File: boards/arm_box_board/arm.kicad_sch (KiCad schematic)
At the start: 5 parts, among them J1 Output, J2 24V, U1 Teensy4.1, U2 PololuD24V5F5, U3 TMC2209_SILENTSTEPSTICK

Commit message: Updated Arm board with ethernet
updated on 04/24
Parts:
- added C1: C_Small, Capacitor_THT:C_Rect_L4.0mm_W2.5mm_P2.50mm, symbol Device:C_Small
- added J3: J00-0045NL, EthernetConn:PULSE_J00-0045NL, symbol EthernetHead:J00-0045NL
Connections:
- net at U1.60 (R+): now also J3.4 (CTT)
- net at U1.61 (LED): now also J3.10 (LC)
- net at U1.62 (T-): now also J3.3 (RD+)
- net at U1.63 (T+): now also J3.1 (TD+)
- net at U1.64 (GND): now also C1.2, J3.8 (GND), J3.9 (LA)
- net at U1.65 (R-): now also J3.6 (RD-)
- new net: C1.1, J3.2 (TD-), J3.5 (CTR)

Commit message: update
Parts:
- C1: footprint Capacitor_THT:C_Rect_L4.0mm_W2.5mm_P2.50mm -> Capacitor_THT:C_Disc_D3.0mm_W1.6mm_P2.50mm
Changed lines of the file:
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@@
 			)
 		)
-		(property "Footprint" "Capacitor_THT:C_Rect_L4.0mm_W2.5mm_P2.50mm"
+		(property "Footprint" "Capacitor_THT:C_Disc_D3.0mm_W1.6mm_P2.50mm"
 			(at 167.64 132.08 0)
 			(effects

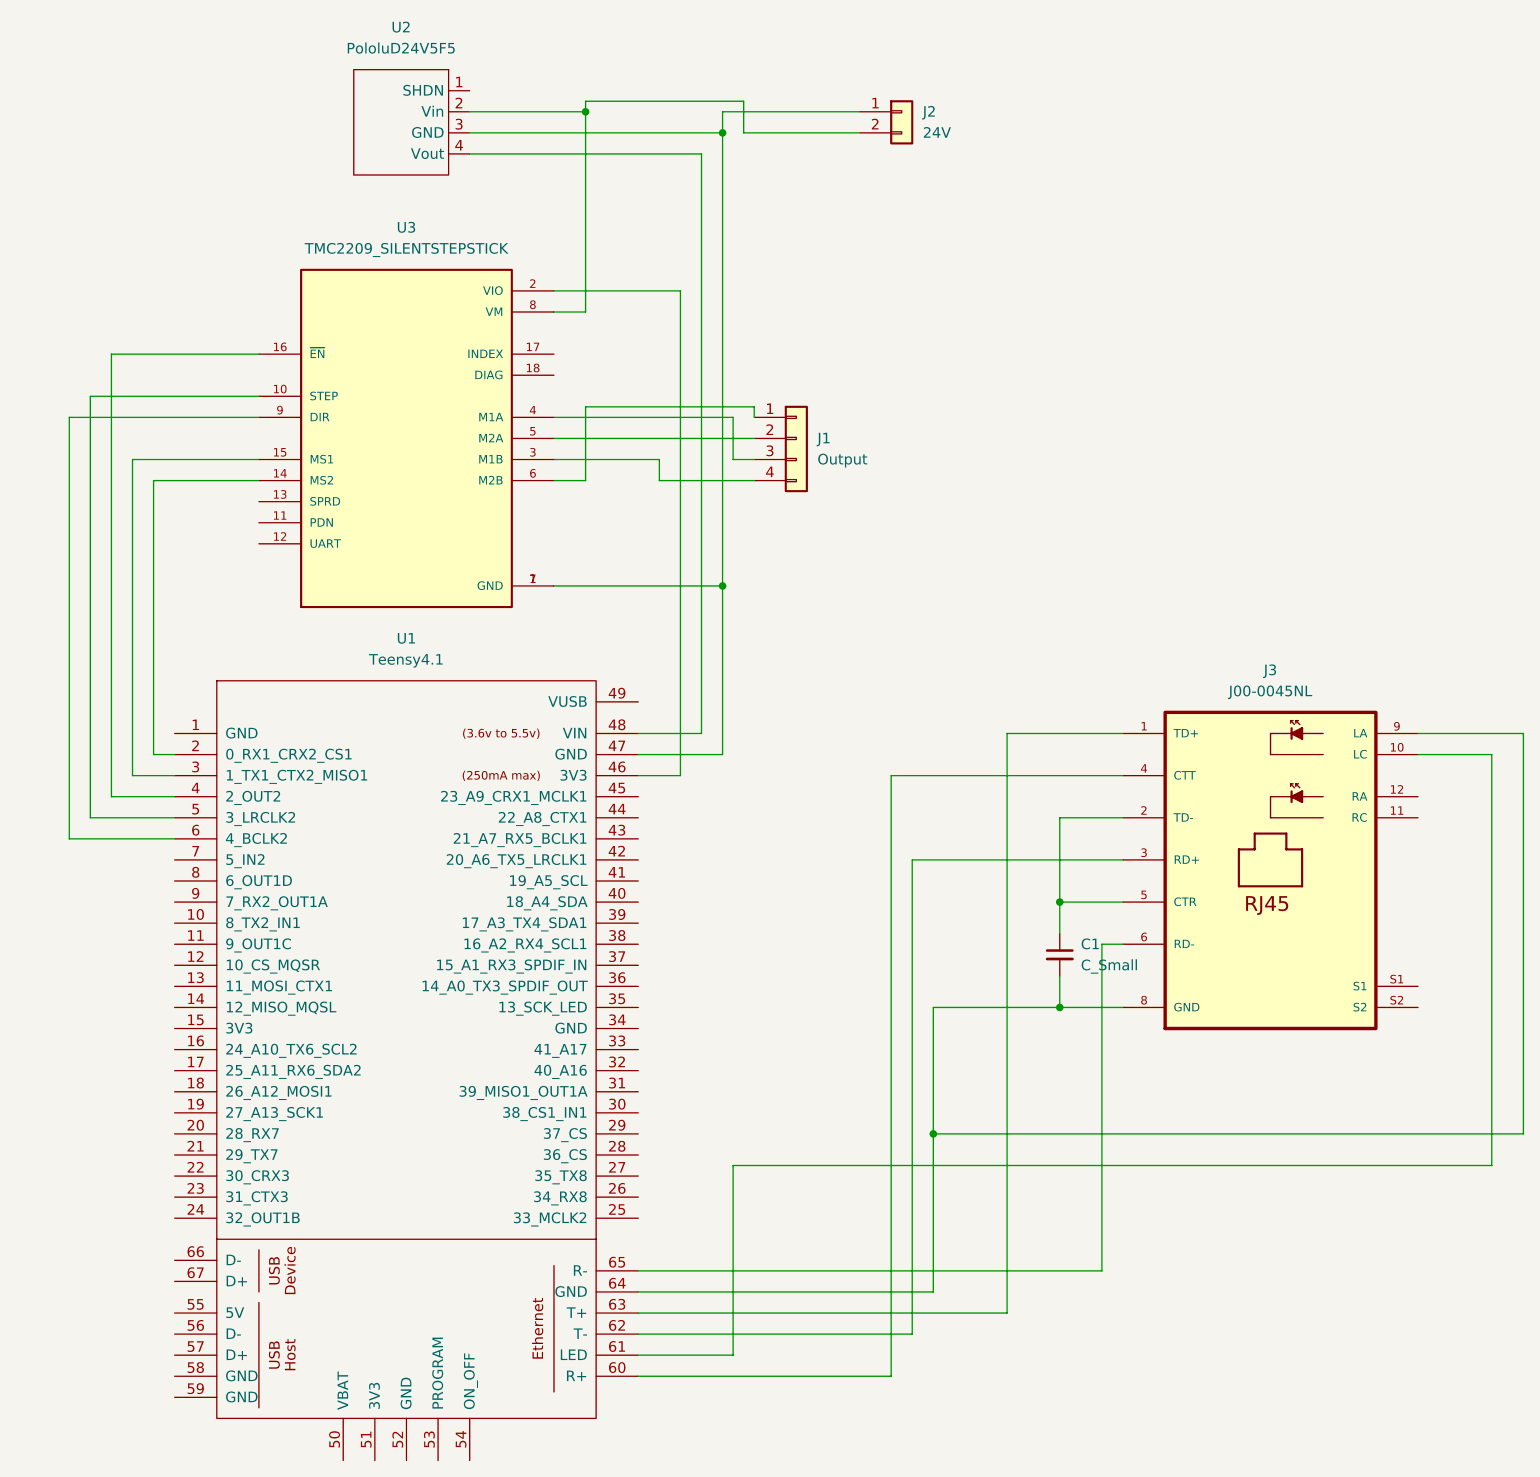
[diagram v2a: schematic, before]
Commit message: Corrected Ethernet pin matches to teensy
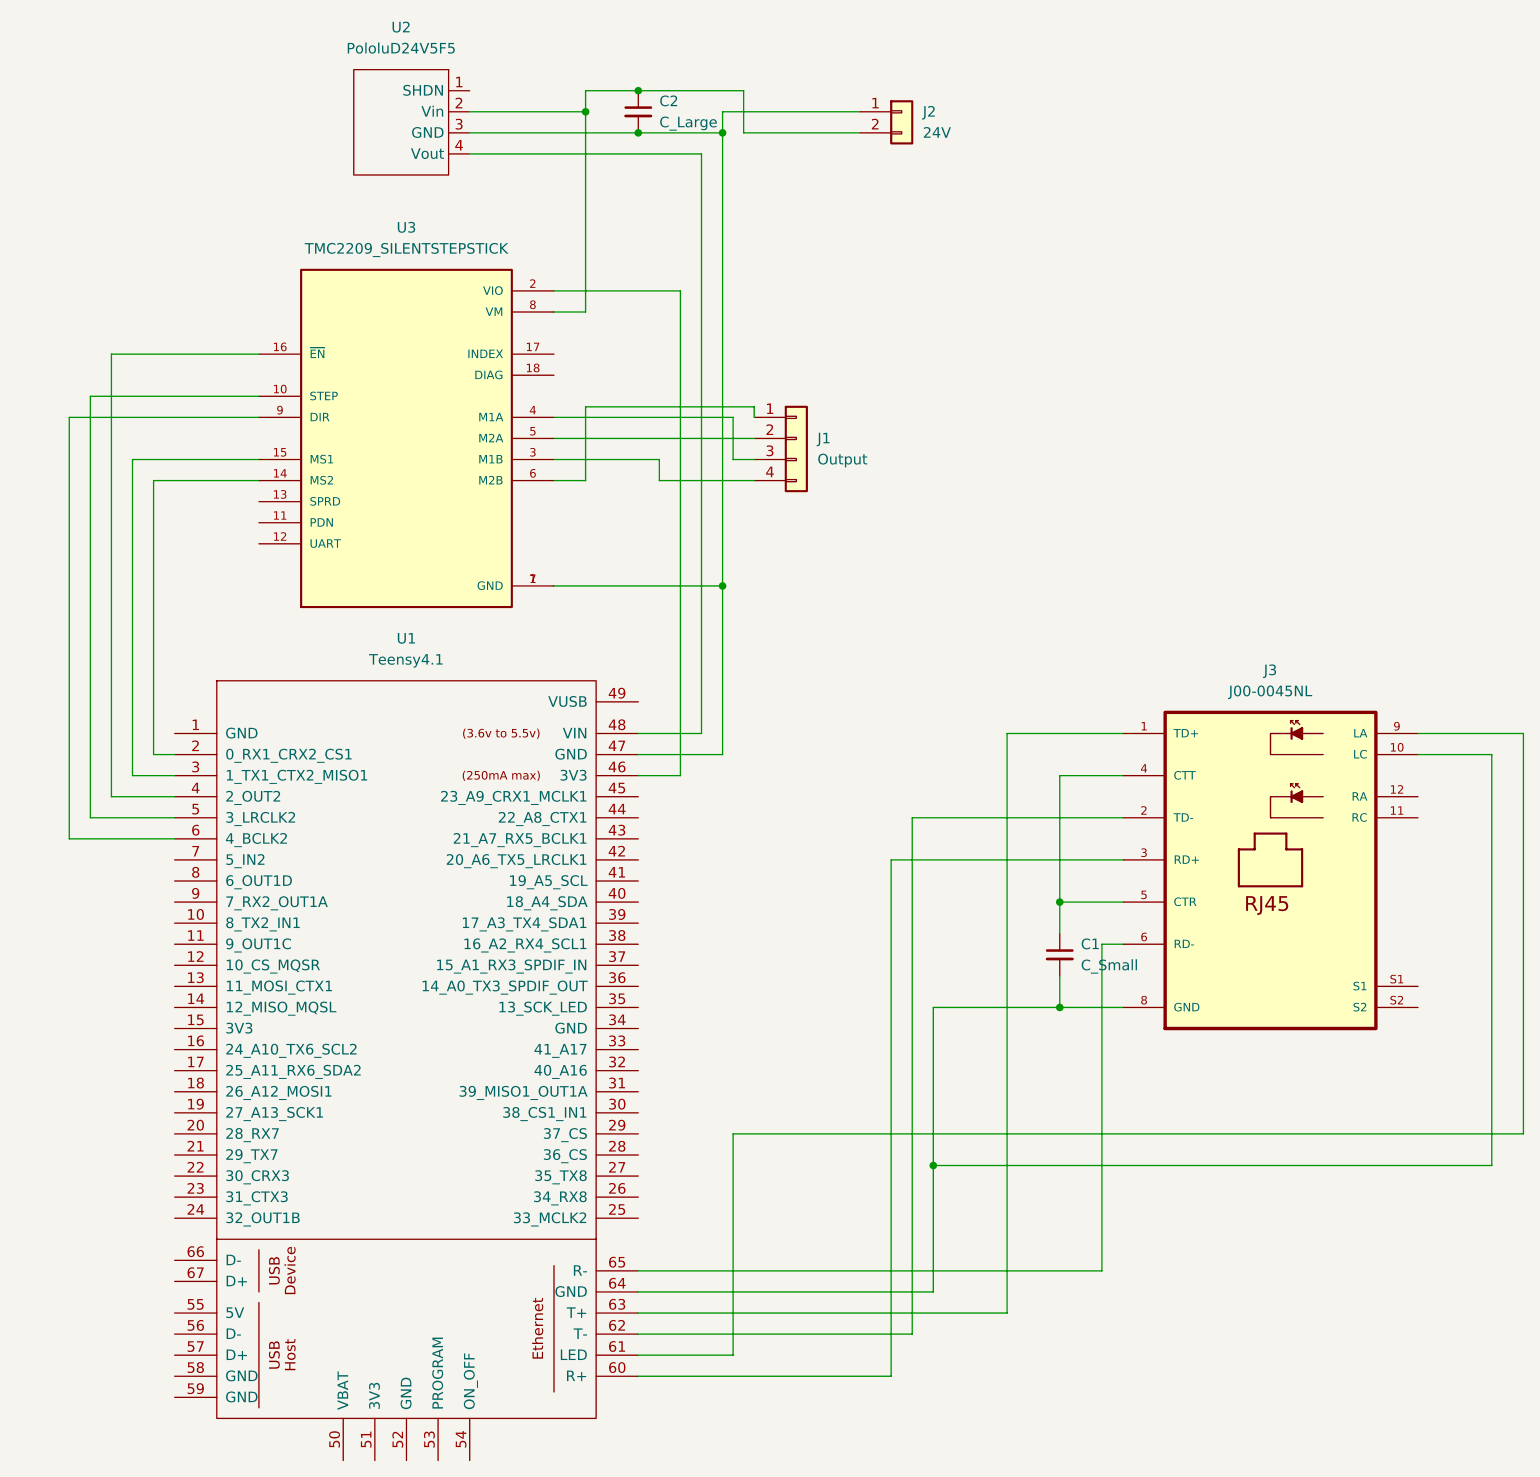
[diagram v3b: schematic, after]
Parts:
- added C2: C_Large, Capacitor_THT:CP_Radial_D4.0mm_P1.50mm, symbol Device:C_Small
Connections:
- net at J2.1 (Pin_1), U1.47 (GND), U2.3 (GND)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: now also C2.2
- net at J2.2 (Pin_2), U2.2 (Vin), U3.8 (VM): now also C2.1
- net at U1.60 (R+): now also J3.3 (RD+); no longer J3.4 (CTT)
- net at U1.61 (LED): now also J3.9 (LA); no longer J3.10 (LC)
- net at U1.62 (T-): now also J3.2 (TD-); no longer J3.3 (RD+)
- net at C1.2, J3.8 (GND), U1.64 (GND): now also J3.10 (LC); no longer J3.9 (LA)
- net at C1.1, J3.5 (CTR): now also J3.4 (CTT); no longer J3.2 (TD-)
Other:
- company: (none) -> RoboNav

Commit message: Extra pins/labels added
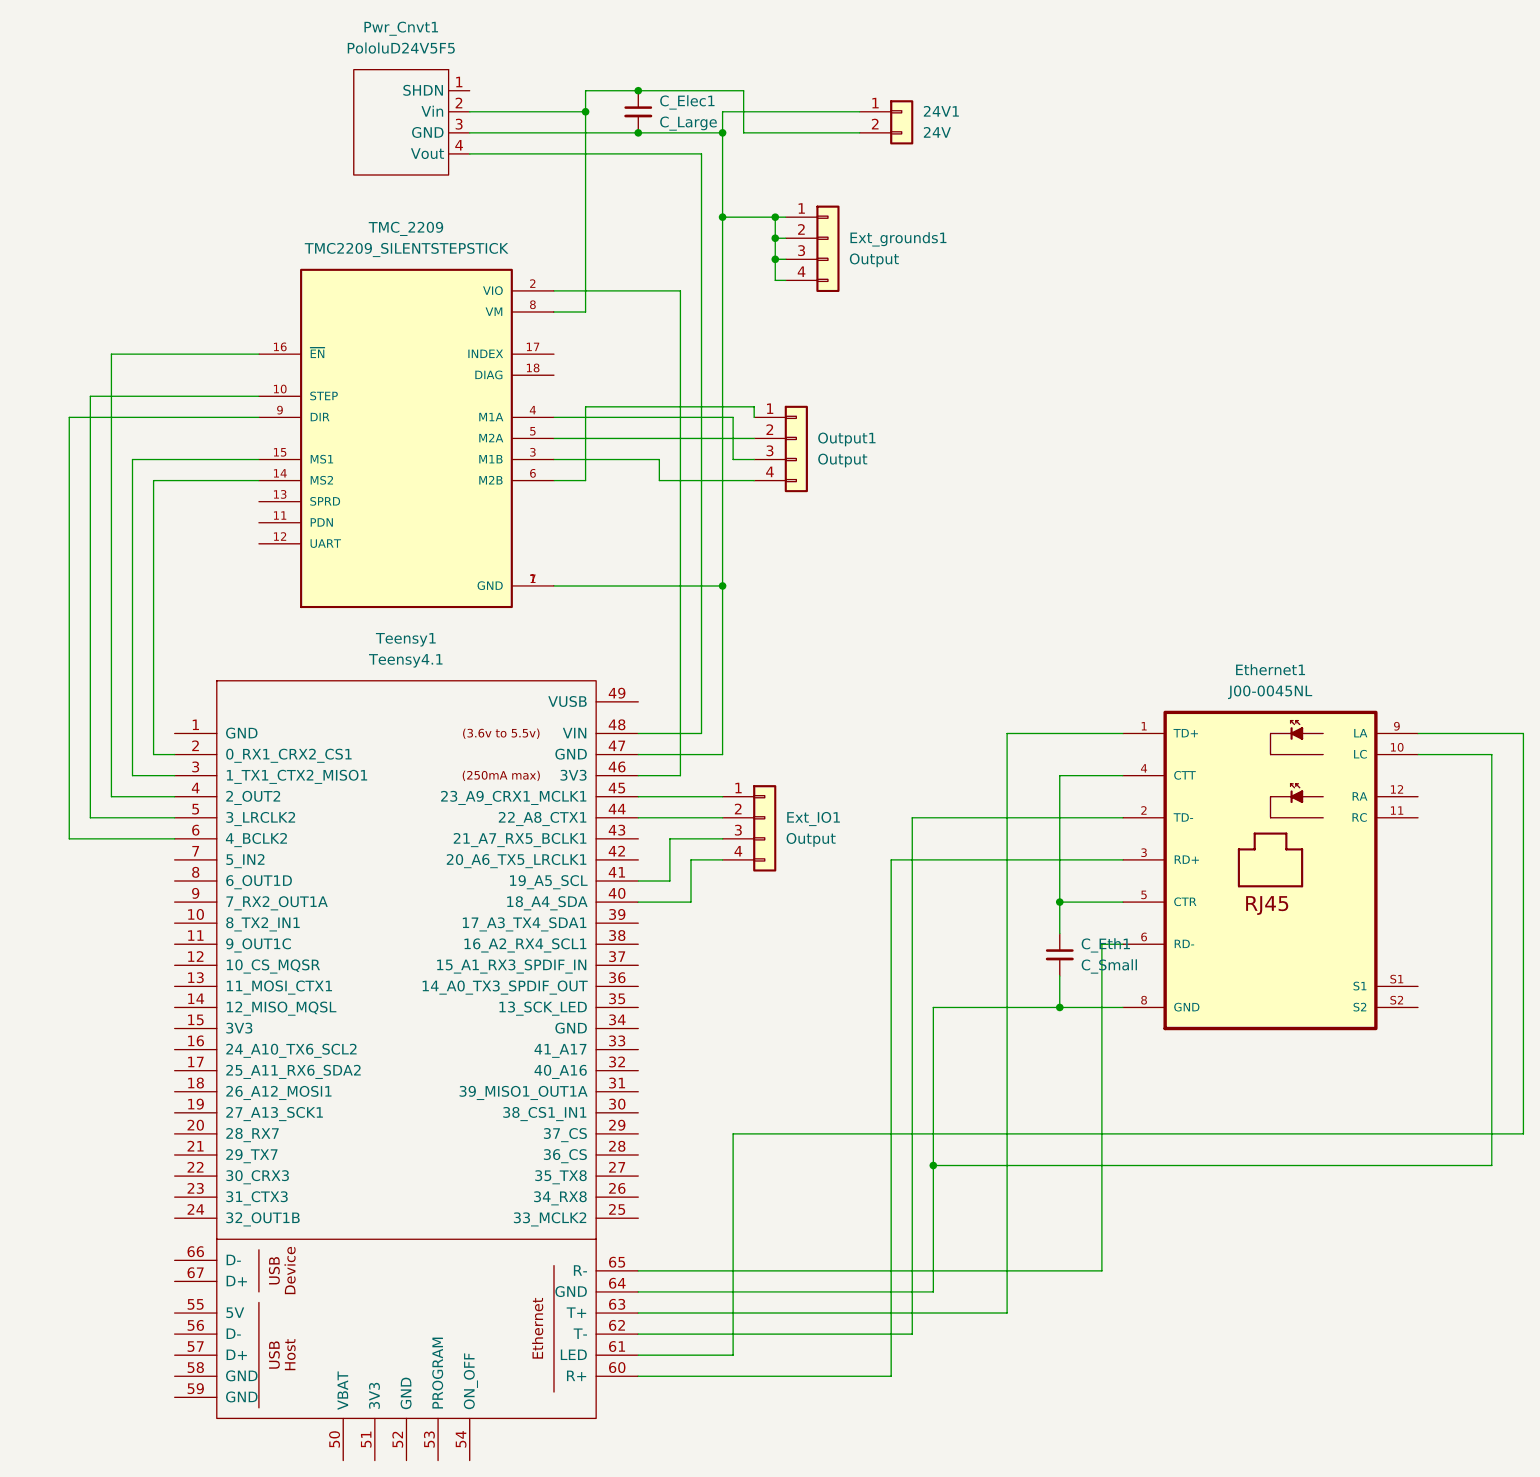
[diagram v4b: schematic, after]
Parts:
- added Ext_IO1, Ext_grounds1: Output, Connector_PinHeader_2.54mm:PinHeader_1x04_P2.54mm_Vertical, symbol Connector_Generic:Conn_01x04
- renumbered J2 to 24V1, C2 to C_Elec1, C1 to C_Eth1, J3 to Ethernet1, J1 to Output1, U2 to Pwr_Cnvt1, U3 to TMC_2209, U1 to Teensy1
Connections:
- net at 24V1.1 (Pin_1), C_Elec1.2, Pwr_Cnvt1.3 (GND)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: now also Ext_grounds1.1 (Pin_1), Ext_grounds1.2 (Pin_2), Ext_grounds1.3 (Pin_3), Ext_grounds1.4 (Pin_4)
- net at Teensy1.40 (18_A4_SDA): now also Ext_IO1.4 (Pin_4)
- net at Teensy1.41 (19_A5_SCL): now also Ext_IO1.3 (Pin_3)
- net at Teensy1.44 (22_A8_CTX1): now also Ext_IO1.2 (Pin_2)
- net at Teensy1.45 (23_A9_CRX1_MCLK1): now also Ext_IO1.1 (Pin_1)

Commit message: Changes to Science and Arm Board
Added pin labels to both boards
Fixed Mislabeled Stepper Board Footprint in Arm board
Added extra digital pins and ground in Science Board
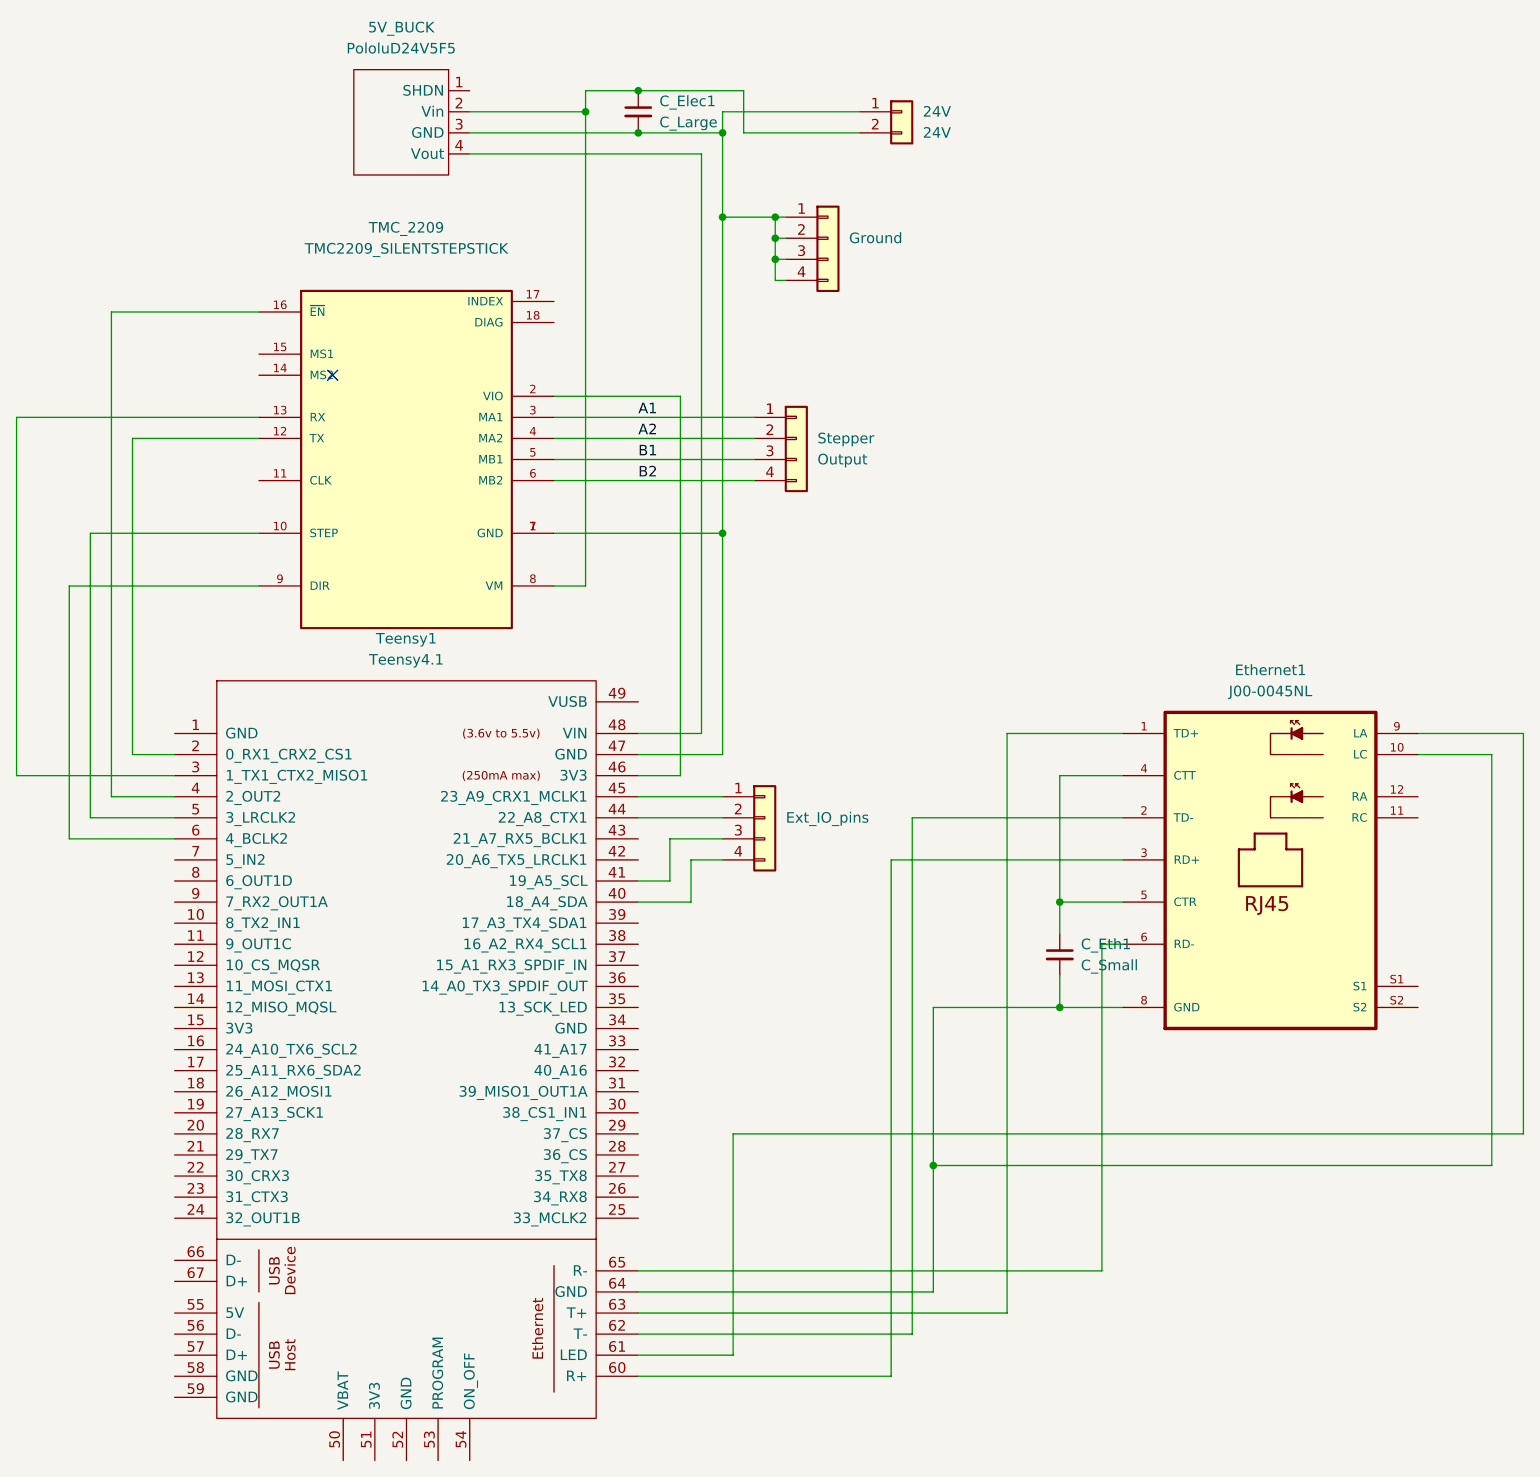
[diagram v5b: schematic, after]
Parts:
- TMC_2209: footprint Bigtreetech_TMC2209:MODULE_TMC2209_SILENTSTEPSTICK -> (none); Availability In Stock -> (none); Check_prices https://www.snapeda.com/parts/TMC2209%20SILENTSTEPSTICK/Tri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 -> (none); Description_1 TMC2209 Motor Controller/Driver Power Management Evaluation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 -> (none); MANUFACTURER Trinamic Motion Control GmbH -> (none); MF Trinamic Motion Control GmbH -> (none); MP TMC2209 SILENTSTEPSTICK -> (none); PARTREV 1.20 -> (none); Package None -> (none); Price None -> (none); STANDARD Manufacturer Recommendations -> (none); SnapEDA_Link https://www.snapeda.com/parts/TMC2209%20SILENTSTEPSTICK/Tri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 -> (none)
- renumbered 24V1 to 24V, Pwr_Cnvt1 to 5V_BUCK, Ext_IO1 to Ext_IO_pins, Ext_grounds1 to Ground, Output1 to Stepper
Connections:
- net at TMC_2209.12 (TX): now also Teensy1.2 (0_RX1_CRX2_CS1)
- net at TMC_2209.13 (RX): now also Teensy1.3 (1_TX1_CTX2_MISO1)
- net at TMC_2209.14 (MS2): no longer Teensy1.2 (0_RX1_CRX2_CS1)
- net at TMC_2209.15 (MS1): no longer Teensy1.3 (1_TX1_CTX2_MISO1)
- net A1: now reaches TMC_2209.3 (MA1)
- net A1: now also Stepper.1 (Pin_1); no longer Stepper.4 (Pin_4)
- net A2: now reaches TMC_2209.4 (MA2)
- net A2: now also Stepper.2 (Pin_2); no longer Stepper.3 (Pin_3)
- net B1: now reaches TMC_2209.5 (MB1)
- net B1: now also Stepper.3 (Pin_3); no longer Stepper.2 (Pin_2)
- net B2: now reaches TMC_2209.6 (MB2)
- net B2: now also Stepper.4 (Pin_4); no longer Stepper.1 (Pin_1)
- no-connect marks 0 -> 1
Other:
- moved on the sheet: TMC_2209
